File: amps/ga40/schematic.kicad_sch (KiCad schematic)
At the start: 41 parts, among them T1 Gibson (no number printed), T2 Gibson (no number printed)

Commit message: Fix: deterministic schematic ids and wires split at every join
- _u() is uuid5 over (amp id, emission order), so a regeneration of an
  unchanged script is byte-identical and a drift gate becomes possible
- write() splits wire segments at symbol pins, wire ends and junction dots,
  so the file connects exactly what the drawing shows under KiCad's
  endpoint-only semantics (270 pins were on a wire's interior; net
  partitions unchanged on all 38 sheets)
- all sheets regenerated; aa864-bassman title block was stale (draft) and
  now matches meta.yaml (verified)

Co-Authored-By: Claude Fable 5.1 <noreply@anthropic.com>
Claude-Session: https://claude.ai/code/session_01KBMfdh37HmCL2iWcBiL5J1
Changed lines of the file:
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@@
   (wire (pts (xy 57.146 55.32) (xy 67.336 55.32))
     (stroke (width 0) (type default)))
-  (wire (pts (xy 67.336 43.32) (xy 67.336 55.32))
+  (wire (pts (xy 67.336 43.32) (xy 67.336 49.32))
+    (stroke (width 0) (type default)))
+  (wire (pts (xy 67.336 49.32) (xy 67.336 55.32))
     (stroke (width 0) (type default)))
   (junction (at 67.336 43.32) (diameter 0) (color 0 0 0 0))
@@
     (property "Reference" "RS1" (at 114.136 42.05 270) (effects (font (size 1.27 1.27)) (justify left)))
     (property "Value" "750k" (at 114.136 44.45 270) (effects (font (size 1.27 1.27)) (justify left))))
-  (wire (pts (xy 98.956 48.05) (xy 113.526 48.05))
+  (wire (pts (xy 98.956 48.05) (xy 105.336 48.05))
+    (stroke (width 0) (type default)))
+  (wire (pts (xy 105.336 48.05) (xy 113.526 48.05))
     (stroke (width 0) (type default)))
   (wire (pts (xy 121.146 48.05) (xy 129.336 48.05))
@@
   (wire (pts (xy 121.146 37.32) (xy 129.336 37.32))
     (stroke (width 0) (type default)))
-  (wire (pts (xy 129.336 37.32) (xy 129.336 53.32))
+  (wire (pts (xy 129.336 37.32) (xy 129.336 48.05))
+    (stroke (width 0) (type default)))
+  (wire (pts (xy 129.336 48.05) (xy 129.336 53.32))
     (stroke (width 0) (type default)))
   (wire (pts (xy 129.336 53.32) (xy 144.416 53.32))
@@
   (global_label "GND" (shape input) (at 211.336 156.94 270)
     (effects (font (size 1.27 1.27)) (justify right)))
-  (wire (pts (xy 201.336 66.22) (xy 273.526 66.22))
+  (wire (pts (xy 201.336 66.22) (xy 221.336 66.22))
+    (stroke (width 0) (type default)))
+  (wire (pts (xy 221.336 66.22) (xy 273.526 66.22))
     (stroke (width 0) (type default)))
   (junction (at 221.336 66.22) (diameter 0) (color 0 0 0 0))
@@
     (property "Reference" "CC1" (at 274.136 60.02 270) (effects (font (size 1.27 1.27)) (justify left)))
     (property "Value" ".02u" (at 274.136 62.42 270) (effects (font (size 1.27 1.27)) (justify left))))
-  (wire (pts (xy 281.146 66.22) (xy 303.716 66.22))
+  (wire (pts (xy 281.146 66.22) (xy 289.336 66.22))
+    (stroke (width 0) (type default)))
+  (wire (pts (xy 289.336 66.22) (xy 303.716 66.22))
     (stroke (width 0) (type default)))
   (symbol (lib_id "cx:PENTODE") (at 311.336 65.585 0) (unit 1)
@@
   (wire (pts (xy 277.336 229.32) (xy 277.336 197.32))
     (stroke (width 0) (type default)))
-  (wire (pts (xy 277.336 197.32) (xy 303.716 197.32))
+  (wire (pts (xy 277.336 197.32) (xy 293.336 197.32))
+    (stroke (width 0) (type default)))
+  (wire (pts (xy 293.336 197.32) (xy 303.716 197.32))
     (stroke (width 0) (type default)))
   (symbol (lib_id "cx:PENTODE") (at 311.336 196.685 0) (unit 1)
@@
   (wire (pts (xy 161.336 181.32) (xy 161.336 189.32))
     (stroke (width 0) (type default)))
-  (wire (pts (xy 145.336 189.32) (xy 161.336 189.32))
+  (wire (pts (xy 145.336 189.32) (xy 153.336 189.32))
+    (stroke (width 0) (type default)))
+  (wire (pts (xy 153.336 189.32) (xy 161.336 189.32))
     (stroke (width 0) (type default)))
   (junction (at 153.336 189.32) (diameter 0) (color 0 0 0 0))

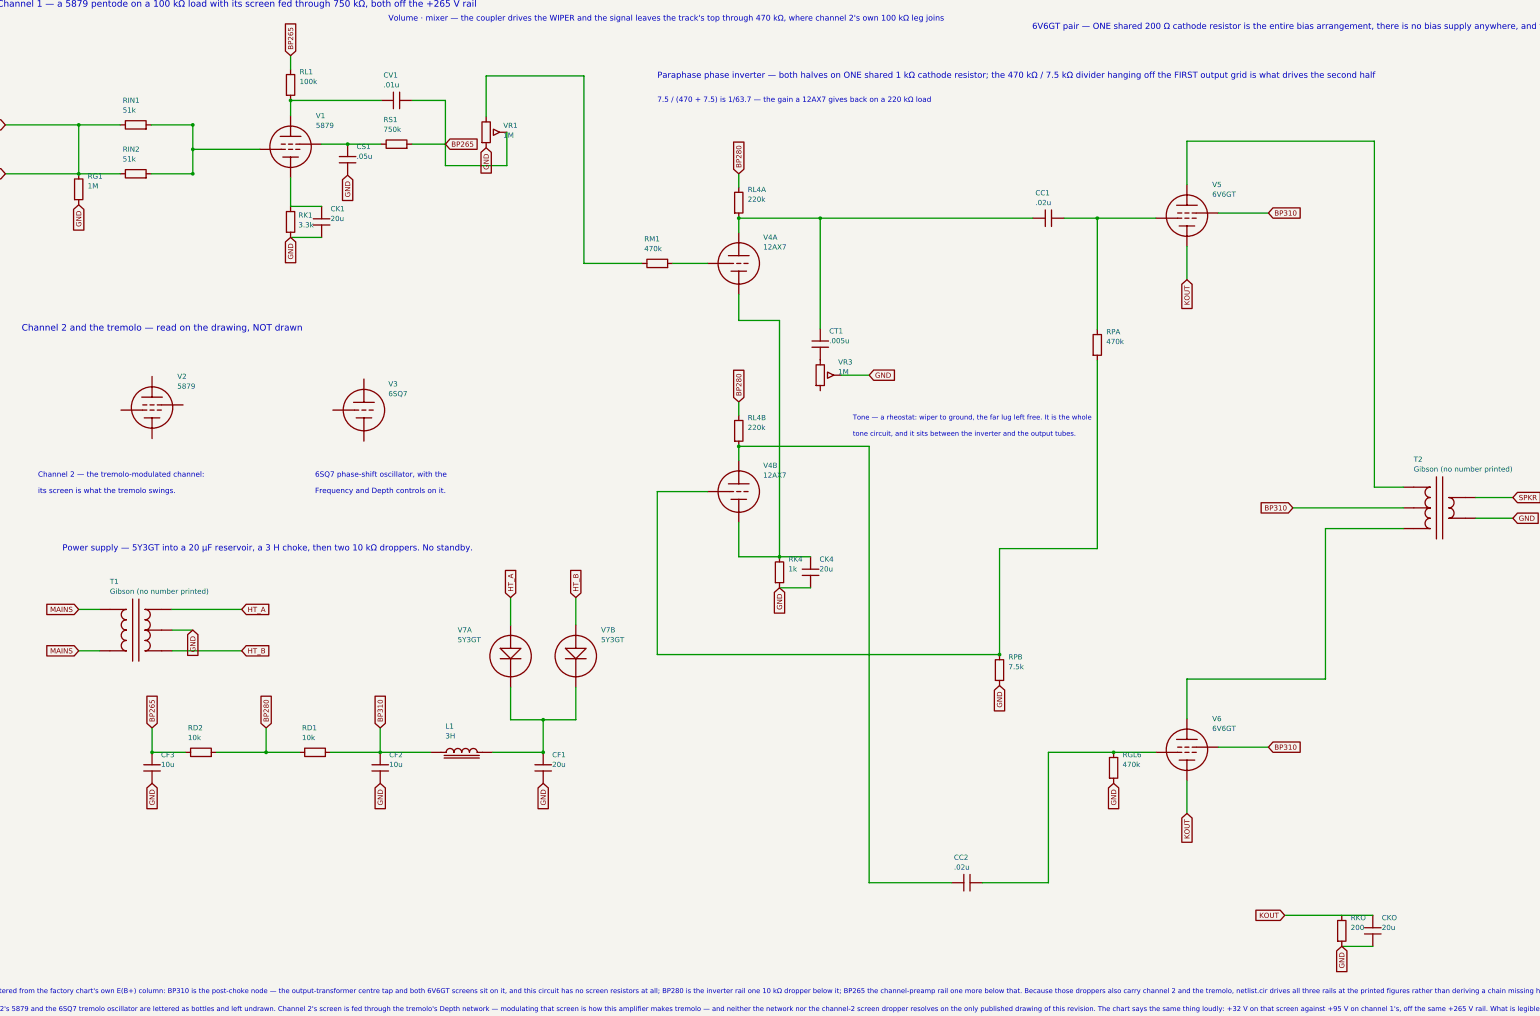
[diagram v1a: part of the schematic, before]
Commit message: Add: real tube pin numbers and readable valve glyphs on every schematic
Phase B of the drawing program. A factory service sheet numbers every tube
pin, because the number is what a technician puts a probe on. This corpus
printed none, and the numbers hidden in its symbols were positional
placeholders (P=1, G=2, K=3) that would have published a 6V6GT's plate as
pin 1 when it is pin 3.

1055 electrodes now carry the real number, 1027 lettered (27 are shared
filaments deduped, 1 dropped for want of clear space on the 6G2). Resolved per
instance from reference/tubes/<slug>.yaml through the same alias resolution the
layout renderer uses, so a 12AX7 section and a 6SL7 section each get their own
basing. A valve whose basing the corpus does not carry prints nothing rather
than a wrong number.

Section letters and basing units are now separate things, which cost a detour
worth recording. The RCA 12AX7-A sheet reads "Pin 1 - Plate of Unit No.2 ...
Pin 6 - Plate of Unit No.1", so unit numbering is not pin order; the 5Y3 and
GZ34 number their units in opposite pin order, so nothing positional can
express it. But the section LETTER is a designator, not a basing fact: this
corpus, like every technician, calls the first stage in signal order V1A, and
five amps' prose already did. On four amps the factory sheets put that first
stage on the other half -- the AA764's own schematic prints +200 V on pin 1 --
so those drawings now state their unit explicitly, each citing its source, and
no letter, netlist, parts list or layout comment changed. 183 layout comments
agree with the printed numbers, 0 disagree. A guard fires if two halves of one
bottle resolve to the same unit, which is exactly how this was found.

Glyphs: the cathode gains a bracket and filament hairpin so it can no longer be
confused with the plate bar, the pentode's screen sits on its own row, and a
rectifier draws as one envelope over its sections instead of two apparent
bottles. Line weights are scaled per sheet to a co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
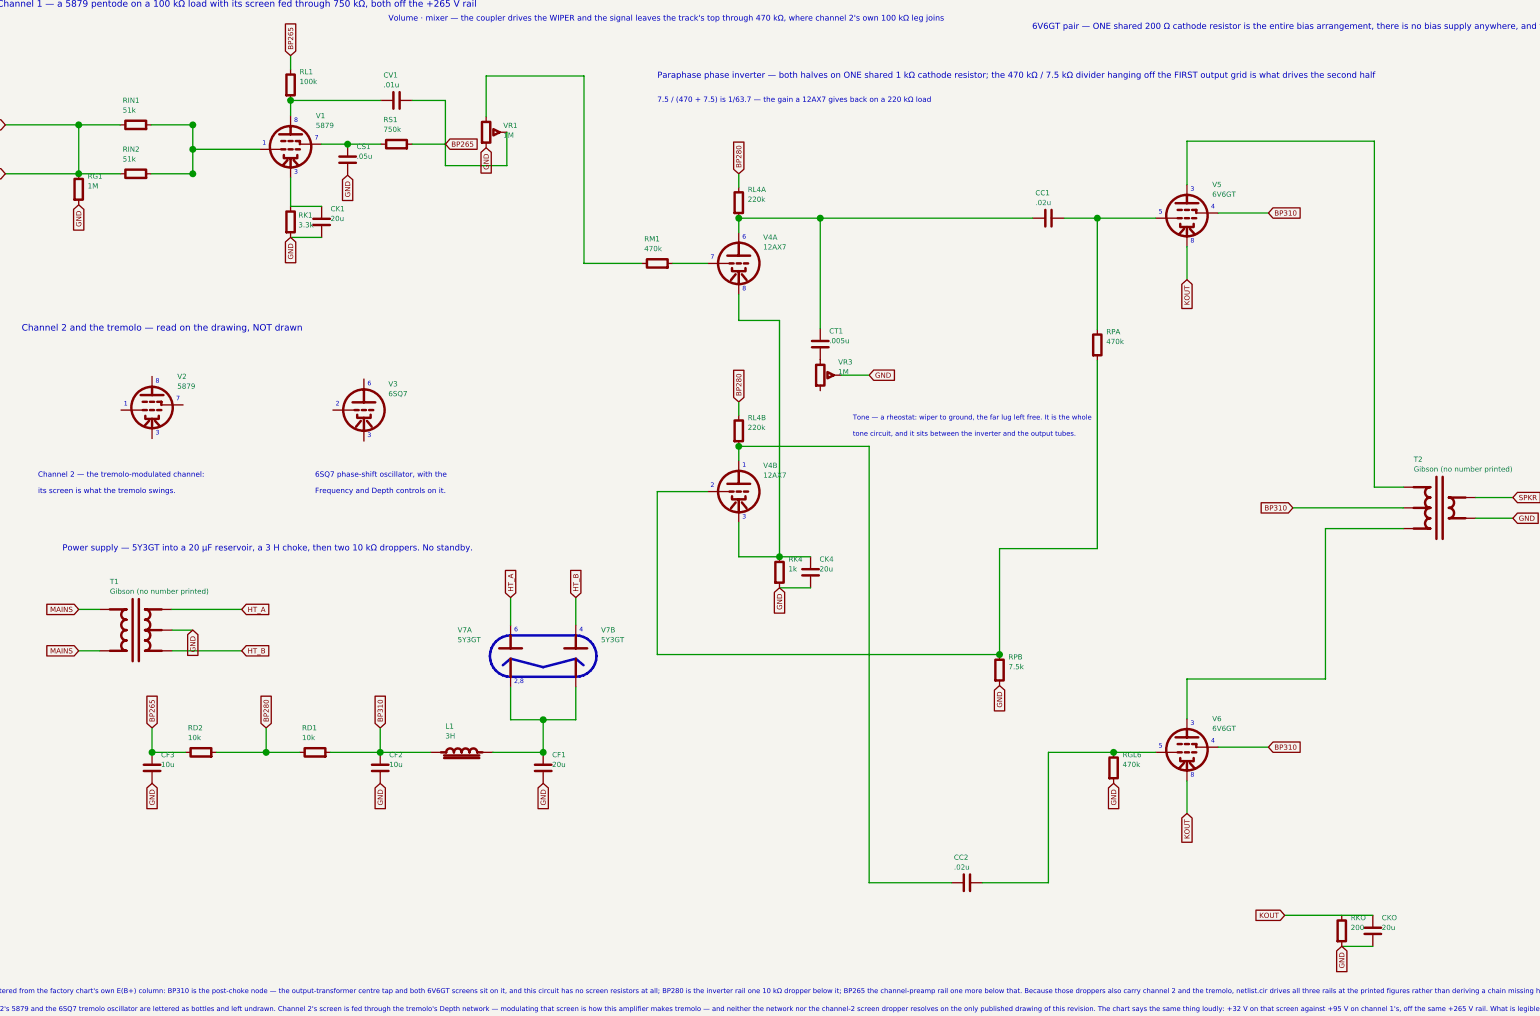
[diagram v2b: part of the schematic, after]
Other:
- note added: "1"
- note added: "2"
- note added: "2,8"
- note added: "3"
- note added: "4"
- note added: "5"
- note added: "6"
- note added: "7"
- note added: "8"
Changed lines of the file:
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@@
   (wire (pts (xy 39.336 43.32) (xy 39.336 55.32))
     (stroke (width 0) (type default)))
-  (junction (at 39.336 43.32) (diameter 0) (color 0 0 0 0))
-  (junction (at 39.336 55.32) (diameter 0) (color 0 0 0 0))
+  (junction (at 39.336 43.32) (diameter 1.7) (color 0 0 0 0))
+  (junction (at 39.336 55.32) (diameter 1.7) (color 0 0 0 0))
   (symbol (lib_id "cx:R") (at 39.336 59.13 0) (unit 1)
     (in_bom yes) (on_board yes)
@@
   (wire (pts (xy 67.336 49.32) (xy 67.336 55.32))
     (stroke (width 0) (type default)))
-  (junction (at 67.336 43.32) (diameter 0) (color 0 0 0 0))
-  (junction (at 67.336 55.32) (diameter 0) (color 0 0 0 0))
-  (junction (at 67.336 49.32) (diameter 0) (color 0 0 0 0))
+  (junction (at 67.336 43.32) (diameter 1.7) (color 0 0 0 0))
+  (junction (at 67.336 55.32) (diameter 1.7) (color 0 0 0 0))
+  (junction (at 67.336 49.32) (diameter 1.7) (color 0 0 0 0))
   (symbol (lib_id "cx:PENTODE") (at 91.336 48.685 0) (unit 1)
     (in_bom yes) (on_board yes)
@@
   (wire (pts (xy 91.336 41.065) (xy 91.336 37.32))
     (stroke (width 0) (type default)))
-  (junction (at 91.336 37.32) (diameter 0) (color 0 0 0 0))
+  (junction (at 91.336 37.32) (diameter 1.7) (color 0 0 0 0))
   (symbol (lib_id "cx:R") (at 91.336 33.51 0) (unit 1)
     (in_bom yes) (on_board yes)
@@
   (global_label "BP265" (shape input) (at 129.336 48.05 0)
     (effects (font (size 1.27 1.27)) (justify left)))
-  (junction (at 105.336 48.05) (diameter 0) (color 0 0 0 0))
+  (junction (at 105.336 48.05) (diameter 1.7) (color 0 0 0 0))
   (symbol (lib_id "cx:C") (at 105.336 51.86 0) (unit 1)
     (in_bom yes) (on_board yes)
@@
   (wire (pts (xy 201.336 69.7) (xy 201.336 66.22))
     (stroke (width 0) (type default)))
-  (junction (at 201.336 66.22) (diameter 0) (color 0 0 0 0))
+  (junction (at 201.336 66.22) (diameter 1.7) (color 0 0 0 0))
   (symbol (lib_id "cx:R") (at 201.336 62.41 0) (unit 1)
     (in_bom yes) (on_board yes)
@@
   (wire (pts (xy 201.336 125.7) (xy 201.336 122.22))
     (stroke (width 0) (type default)))
-  (junction (at 201.336 122.22) (diameter 0) (color 0 0 0 0))
+  (junction (at 201.336 122.22) (diameter 1.7) (color 0 0 0 0))
   (symbol (lib_id "cx:R") (at 201.336 118.41 0) (unit 1)
     (in_bom yes) (on_board yes)
@@
   (wire (pts (xy 201.336 149.32) (xy 211.336 149.32))
     (stroke (width 0) (type default)))
-  (junction (at 211.336 149.32) (diameter 0) (color 0 0 0 0))
+  (junction (at 211.336 149.32) (diameter 1.7) (color 0 0 0 0))
   (symbol (lib_id "cx:R") (at 211.336 153.13 0) (unit 1)
     (in_bom yes) (on_board yes)
@@
   (wire (pts (xy 221.336 66.22) (xy 273.526 66.22))
     (stroke (width 0) (type default)))
-  (junction (at 221.336 66.22) (diameter 0) (color 0 0 0 0))
+  (junction (at 221.336 66.22) (diameter 1.7) (color 0 0 0 0))
   (wire (pts (xy 221.336 66.22) (xy 221.336 93.32))
     (stroke (width 0) (type default)))
@@
     (property "Reference" "V5" (at 317.536 57.985 0) (effects (font (size 1.27 1.27)) (justify left)))
     (property "Value" "6V6GT" (at 317.536 60.385 0) (effects (font (size 1.27 1.27)) (justify left))))
-  (junction (at 289.336 66.22) (diameter 0) (color 0 0 0 0))
+  (junction (at 289.336 66.22) (diameter 1.7) (color 0 0 0 0))
   (wire (pts (xy 289.336 66.22) (xy 289.336 93.51))
     (stroke (width 0) (type default)))
@@
   (wire (pts (xy 265.336 147.32) (xy 265.336 173.32))
     (stroke (width 0) (type default)))
-  (junction (at 265.336 173.32) (diameter 0) (color 0 0 0 0))
+  (junction (at 265.336 173.32) (diameter 1.7) (color 0 0 0 0))
   (symbol (lib_id "cx:R") (at 265.336 177.13 0) (unit 1)
     (in_bom yes) (on_board yes)
@@
     (property "Reference" "V6" (at 317.536 189.085 0) (effects (font (size 1.27 1.27)) (justify left)))
     (property "Value" "6V6GT" (at 317.536 191.485 0) (effects (font (size 1.27 1.27)) (justify left))))
-  (junction (at 293.336 197.32) (diameter 0) (color 0 0 0 0))
+  (junction (at 293.336 197.32) (diameter 1.7) (color 0 0 0 0))
   (symbol (lib_id "cx:R") (at 293.336 201.13 0) (unit 1)
     (in_bom yes) (on_board yes)
@@
   (wire (pts (xy 153.336 189.32) (xy 161.336 189.32))
     (stroke (width 0) (type default)))
-  (junction (at 153.336 189.32) (diameter 0) (color 0 0 0 0))
+  (junction (at 153.336 189.32) (diameter 1.7) (color 0 0 0 0))
   (wire (pts (xy 153.336 189.32) (xy 153.336 197.32))
     (stroke (width 0) (type default)))
-  (junction (at 153.336 197.32) (diameter 0) (color 0 0 0 0))
+  (junction (at 153.336 197.32) (diameter 1.7) (color 0 0 0 0))
   (symbol (lib_id "cx:C") (at 153.336 201.13 0) (unit 1)
     (in_bom yes) (on_board yes)
@@
   (wire (pts (xy 125.716 197.32) (xy 113.336 197.32))
     (stroke (width 0) (type default)))
-  (junction (at 113.336 197.32) (diameter 0) (color 0 0 0 0))
+  (junction (at 113.336 197.32) (diameter 1.7) (color 0 0 0 0))
   (symbol (lib_id "cx:C") (at 113.336 201.13 0) (unit 1)
     (in_bom yes) (on_board yes)
@@
   (wire (pts (xy 93.526 197.32) (xy 85.336 197.32))
     (stroke (width 0) (type default)))
-  (junction (at 85.336 197.32) (diameter 0) (color 0 0 0 0))
+  (junction (at 85.336 197.32) (diameter 1.7) (color 0 0 0 0))
   (wire (pts (xy 85.336 197.32) (xy 85.336 191.32))
     (stroke (width 0) (type default)))
@@
   (wire (pts (xy 65.526 197.32) (xy 57.336 197.32))
     (stroke (width 0) (type default)))
-  (junction (at 57.336 197.32) (diameter 0) (color 0 0 0 0))
+  (junction (at 57.336 197.32) (diameter 1.7) (color 0 0 0 0))
   (symbol (lib_id "cx:C") (at 57.336 201.13 0) (unit 1)
     (in_bom yes) (on_board yes)
@@
   (global_label "BP265" (shape input) (at 57.336 191.32 90)
     (effects (font (size 1.27 1.27)) (justify left)))
+  (polyline (pts (xy 161.336 168.62) (xy 162.327 168.718) (xy 163.28 169.007) (xy 164.158 169.476) (xy 164.928 170.108) (xy 165.56 170.878) (xy 166.029 171.756) (xy 166.318 172.709) (xy 166.416 173.7) (xy 166.318 174.691) (xy 166.029 175.644) (xy 165.56 176.522) (xy 164.928 177.292) (xy 164.158 177.924) (xy 163.28 178.393) (xy 162.327 178.682) (xy 161.336 178.78) (xy 145.336 178.78) (xy 144.345 178.682) (xy 143.392 178.393) (xy 142.514 177.924) (xy 141.744 177.292) (xy 141.112 176.522) (xy 140.643 175.644) (xy 140.354 174.691) (xy 140.256 173.7) (xy 140.354 172.709) (xy 140.643 171.756) (xy 141.112 170.878) (xy 141.744 170.108) (xy 142.514 169.476) (xy 143.392 169.007) (xy 144.345 168.718) (xy 145.336 168.62) (xy 161.336 168.62))
+    (stroke (width 0.603) (type default) (color 197 163 255 1)) (fill (type none)))
+  (polyline (pts (xy 143.436 175.935) (xy 145.336 174.335) (xy 153.336 176.415) (xy 161.336 174.335) (xy 163.236 175.935))
+    (stroke (width 0.603) (type default) (color 197 163 255 1)) (fill (type none)))
+  (text "8" (at 92.186 42.335 0)
+    (effects (font (size 1.1 1.1)) (justify left)))
+  (text "1" (at 84.3888 47.92 0)
+    (effects (font (size 1.1 1.1)) (justify left)))
+  (text "7" (at 97.236 46.65 0)
+    (effects (font (size 1.1 1.1)) (justify left)))
+  (text "3" (at 92.186 55.035 0)
+    (effects (font (size 1.1 1.1)) (justify left)))
+  (text "6" (at 202.186 70.97 0)
+    (effects (font (size 1.1 1.1)) (justify left)))
+  (text "7" (at 194.389 75.92 0)
+    (effects (font (size 1.1 1.1)) (justify left)))
+  (text "8" (at 202.186 83.67 0)
+    (effects (font (size 1.1 1.1)) (justify left)))
+  (text "1" (at 202.186 126.97 0)
+    (effects (font (size 1.1 1.1)) (justify left)))
+  (text "2" (at 194.389 131.92 0)
+    (effects (font (size 1.1 1.1)) (justify left)))
+  (text "3" (at 202.186 139.67 0)
+    (effects (font (size 1.1 1.1)) (justify left)))
+  (text "3" (at 312.186 59.235 0)
+    (effects (font (size 1.1 1.1)) (justify left)))
+  (text "5" (at 304.389 64.82 0)
+    (effects (font (size 1.1 1.1)) (justify left)))
+  (text "4" (at 317.236 63.55 0)
+    (effects (font (size 1.1 1.1)) (justify left)))
+  (text "8" (at 312.186 71.935 0)
+    (effects (font (size 1.1 1.1)) (justify left)))
+  (text "3" (at 312.186 190.335 0)
+    (effects (font (size 1.1 1.1)) (justify left)))
+  (text "5" (at 304.389 195.92 0)
+    (effects (font (size 1.1 1.1)) (justify left)))
+  (text "4" (at 317.236 194.65 0)
+    (effects (font (size 1.1 1.1)) (justify left)))
+  (text "8" (at 312.186 203.035 0)
+    (effects (font (size 1.1 1.1)) (justify left)))
+  (text "8" (at 58.186 106.335 0)
+    (effects (font (size 1.1 1.1)) (justify left)))
+  (text "1" (at 50.3888 111.92 0)
+    (effects (font (size 1.1 1.1)) (justify left)))
+  (text "7" (at 63.236 110.65 0)
+    (effects (font (size 1.1 1.1)) (justify left)))
+  (text "3" (at 58.186 119.035 0)
+    (effects (font (size 1.1 1.1)) (justify left)))
+  (text "6" (at 110.186 106.97 0)
+    (effects (font (size 1.1 1.1)) (justify left)))
+  (text "2" (at 102.389 111.92 0)
+    (effects (font (size 1.1 1.1)) (justify left)))
+  (text "3" (at 110.186 119.67 0)
+    (effects (font (size 1.1 1.1)) (justify left)))
+  (text "6" (at 146.186 167.35 0)
+    (effects (font (size 1.1 1.1)) (justify left)))
+  (text "2,8" (at 146.186 180.05 0)
+    (effects (font (size 1.1 1.1)) (justify left)))
+  (text "4" (at 162.186 167.35 0)
+    (effects (font (size 1.1 1.1)) (justify left)))
   (text "Rails, lettered from the factory chart's own E(B+) column: BP310 is the post-choke node — the output-transformer centre tap and both 6V6GT screens sit on it, and this circuit has no screen resistors at all; BP280 is the inverter rail one 10 kΩ dropper below it; BP265 the channel-preamp rail one more below that. Because those droppers also carry channel 2 and the tremolo, netlist.cir drives all three rails at the printed figures rather than deriving a chain missing half its load." (at 12.7 256.098 0)
     (effects (font (size 1.2 1.2)) (justify left)))
